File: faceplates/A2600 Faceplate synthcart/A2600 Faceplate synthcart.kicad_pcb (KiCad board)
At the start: 2 copper layers, 61 x 99.7 mm, 54 parts, among them M1 Mounting, M2 Mounting, M3 Mounting, M4 Mounting

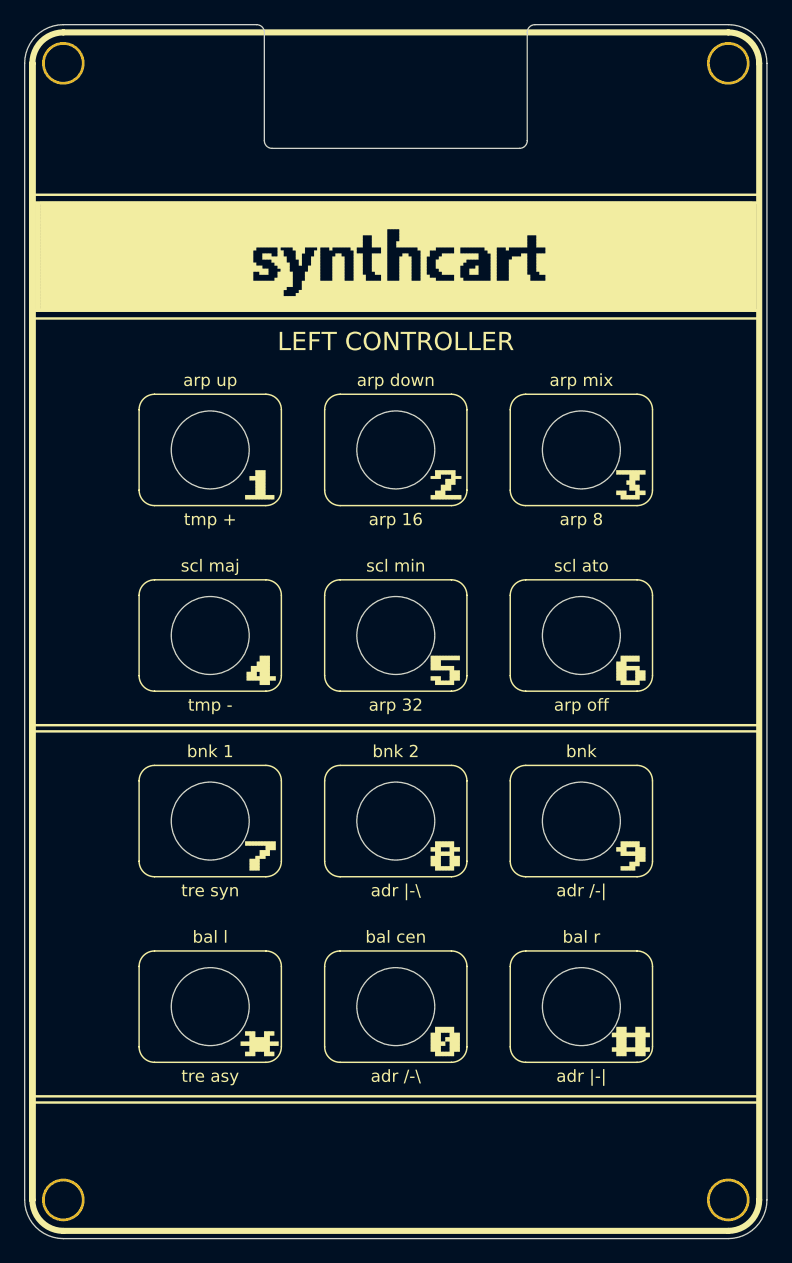
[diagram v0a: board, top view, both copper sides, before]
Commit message: Updated gerber files after tweaking font sizes
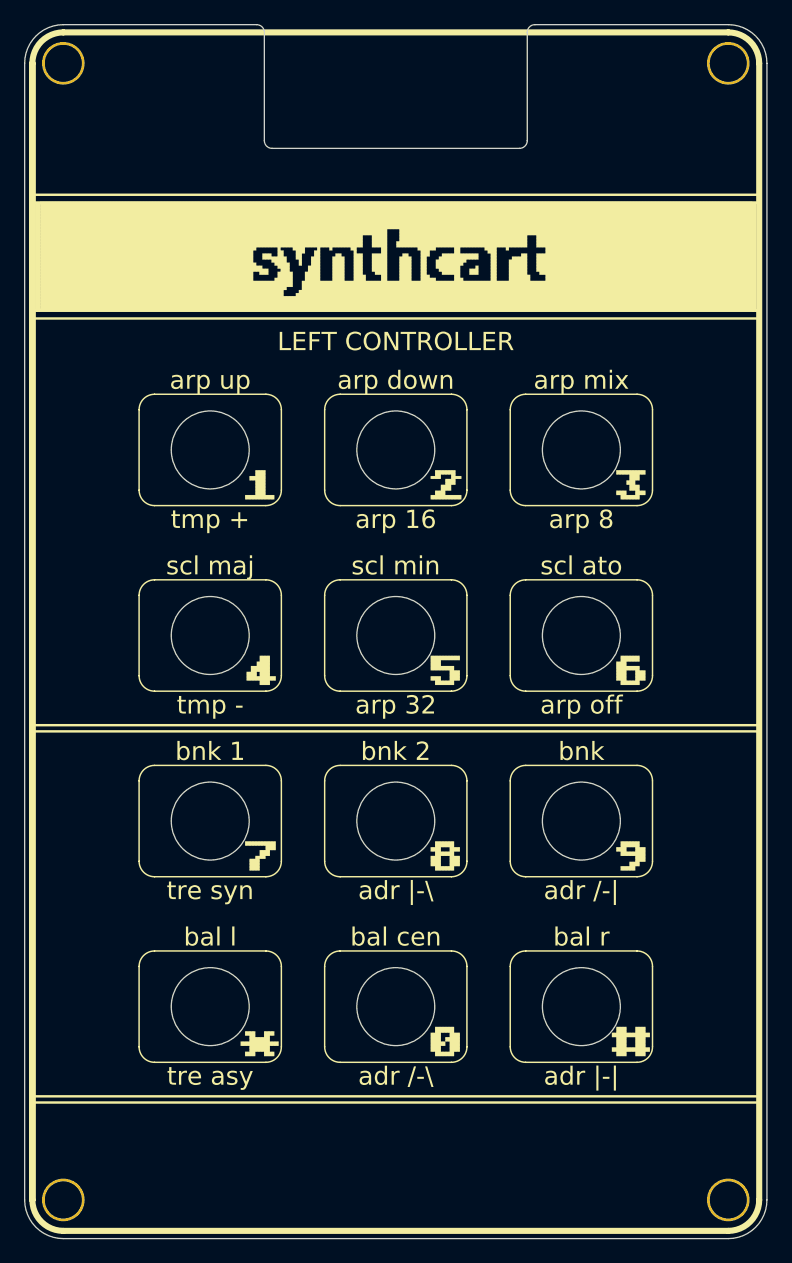
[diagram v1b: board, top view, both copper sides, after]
